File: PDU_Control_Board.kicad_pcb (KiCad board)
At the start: 4 copper layers, 237.7 x 87.4 mm, 221 parts, among them J1 Current_Sensor, J10 Precharge_2, J11 Shunt_2, J12 VIN_Enable, J13 To_Main_Connector, J2 Shunt_1, J20 VDC_IN, J21 VDC_OUT1, J22 VDC_OUT2, J3 SWD, J4 Precharge_1, J5 Precharge_2, J6 Shunt_2, J7 VIN_Enable, J8 Precharge_1, J9 Shunt_1, Q1 BSP75N, Q10 BC817, Q2 BSP75N, Q3 BSP75N, Q4 BSP75N, Q5 BSP75N, Q6 BC817, Q7 BC817, Q8 BC817, Q9 BC817, U1 LMV321, U2 APM32F405xG, U3 LMV321, U4 LMV321, U5 LMV321, U6 LMV321, Y2 X322516MOB4SI

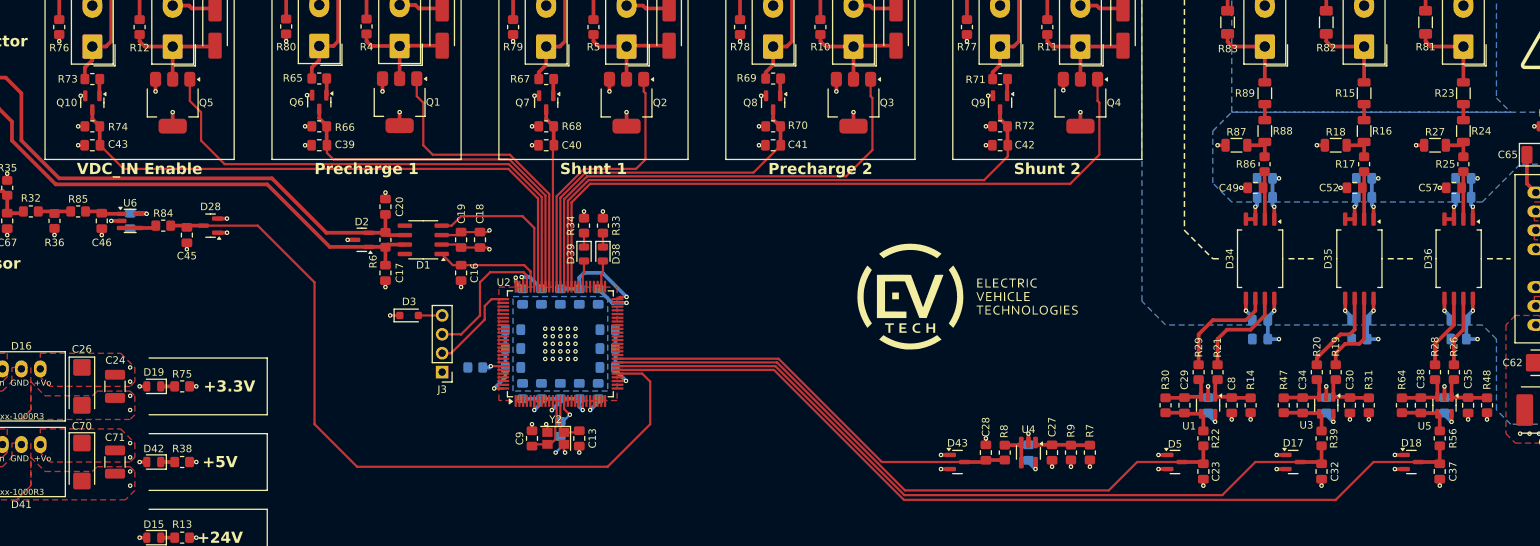
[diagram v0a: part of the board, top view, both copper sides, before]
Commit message: VER3.0: разобрался с бомом, добавил дискреты, DAC, поменял обратную свзять от контакторов, удлинил цепочку измерения высокого
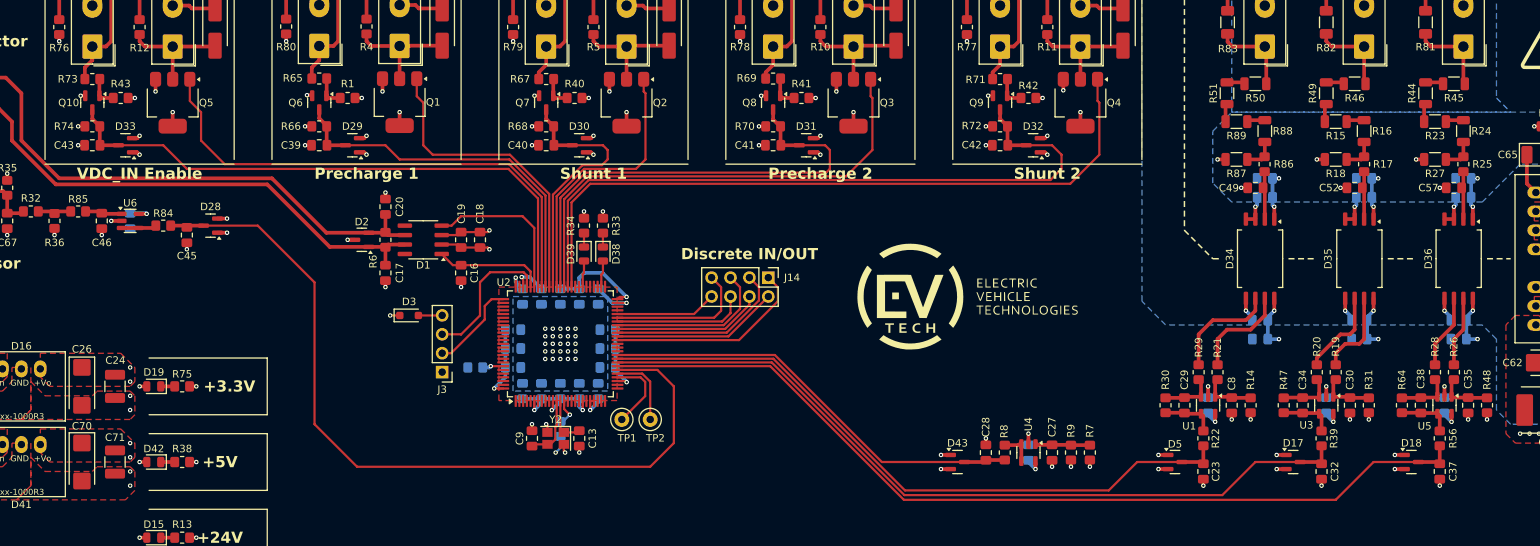
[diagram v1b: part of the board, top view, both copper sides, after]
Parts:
- added D29: ~, Package_TO_SOT_SMD:SOT-23, F.Cu at (282.6, 188.6)
- added D30: ~, Package_TO_SOT_SMD:SOT-23, F.Cu at (313.1, 188.6)
- added D31: ~, Package_TO_SOT_SMD:SOT-23, F.Cu at (343.5, 188.6)
- added D32: ~, Package_TO_SOT_SMD:SOT-23, F.Cu at (374.0, 188.6)
- added D33: ~, Package_TO_SOT_SMD:SOT-23, F.Cu at (252.1, 188.6)
- added J14: ~, Connector_PinHeader_2.54mm:PinHeader_2x04_P2.54mm_Vertical, F.Cu at (338.4, 206.4)
- added R1: 10k, Resistor_SMD:R_0805_2012Metric_Pad1.20x1.40mm_HandSolder, F.Cu at (281.9, 182.2)
- added R40: 10k, Resistor_SMD:R_0805_2012Metric_Pad1.20x1.40mm_HandSolder, F.Cu at (312.4, 182.2)
- added R41: 10k, Resistor_SMD:R_0805_2012Metric_Pad1.20x1.40mm_HandSolder, F.Cu at (342.9, 182.2)
- added R42: 10k, Resistor_SMD:R_0805_2012Metric_Pad1.20x1.40mm_HandSolder, F.Cu at (373.4, 182.2)
- added R43: 10k, Resistor_SMD:R_0805_2012Metric_Pad1.20x1.40mm_HandSolder, F.Cu at (251.5, 182.2)
- added R44: 23.7k, Resistor_SMD:R_1206_3216Metric, F.Cu at (426.7, 181.6)
- added R45: 23.7k, Resistor_SMD:R_1206_3216Metric, F.Cu at (430.5, 180.3)
- added R46: 23.7k, Resistor_SMD:R_1206_3216Metric, F.Cu at (417.2, 180.3)
- added R49: 23.7k, Resistor_SMD:R_1206_3216Metric, F.Cu at (413.4, 181.6)
- added R50: 23.7k, Resistor_SMD:R_1206_3216Metric, F.Cu at (403.9, 180.3)
- added R51: 23.7k, Resistor_SMD:R_1206_3216Metric, F.Cu at (400.1, 181.6)
- added TP1: TestPoint, TestPoint:TestPoint_Loop_D1.80mm_Drill1.0mm_Beaded, F.Cu at (318.8, 225.4)
- added TP2: TestPoint, TestPoint:TestPoint_Loop_D1.80mm_Drill1.0mm_Beaded, F.Cu at (322.6, 225.4)
- C39, C40, C41, C42, C43: value 2.2u -> 1u
- D1: value SIT65HVD232DR -> ~
- D10, D11, D12, D14, D15, D19, D20, D21, D22, D23, D24, D25, D26, D27, D38, D39, D40, D42, D9: value LED_Small -> ~
- D13, D3, D4, D6, D7, D8: value D_Small -> ~
- D16: value K7803-1000R3 -> ~
- D17, D18, D28, D43, D5: value BAT54S -> ~
- D2: value PESD2CAN -> ~
- D34, D35, D36: value NSI1311 -> ~
- D37: value WRB2403S-3WR2 -> ~
- D41: value K7805-1000R3 -> ~
- J1: value Current_Sensor -> ~
- J10, J5: value Precharge_2 -> ~
- J11, J6: value Shunt_2 -> ~
- J12, J7: value VIN_Enable -> ~
- J13: value To_Main_Connector -> ~
- J2, J9: value Shunt_1 -> ~
- J20: value VDC_IN -> ~
- J21: value VDC_OUT1 -> ~
- J22: value VDC_OUT2 -> ~
- J3: value SWD -> ~
- J4, J8: value Precharge_1 -> ~
- Q1, Q2, Q3, Q4, Q5: value BSP75N -> ~
- Q10, Q6, Q7, Q8, Q9: value BC817 -> ~
- R15, R16, R23, R24, R88, R89: value 47k -> 23.7k
- R18, R27, R87: value 240 -> 210
- R35: value DNP -> 1k
- R65, R67, R69, R71, R73: value 2.2k -> 10k
- R66, R68, R70, R72, R74: value 1k -> 100
- U1, U3, U5, U6: value LMV321 -> ~
- U2: value APM32F405xG -> ~
- U4: value LMV321 -> ~; footprint Package_TO_SOT_SMD:SOT-23-5_HandSoldering -> Package_TO_SOT_SMD:SOT-23-5
- Y2: value X322516MOB4SI -> ~
- moved R15 5.39 mm to (414.7, 185.4), turned to 180 degrees
- moved R23 5.39 mm to (428.0, 185.4), turned to 180 degrees
- moved R89 5.39 mm to (401.3, 185.4), turned to 180 degrees
- moved R18 1.91 mm to (414.7, 190.5)
- moved R27 1.91 mm to (428.0, 190.5)
- moved R87 1.91 mm to (401.3, 190.5)
- moved Q6 0.07 mm to (278.1, 182.9)
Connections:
- C28 pad 1: DC_Voltage_MCU -> +24V_SENSE
- D43 pad 3: DC_Voltage_MCU -> +24V_SENSE
- R15 pad 2: VDC_OUT1 -> Net-(R15-Pad2)
- R23 pad 2: VDC_OUT2 -> Net-(R23-Pad2)
- R8 pad 2: DC_Voltage_MCU -> +24V_SENSE
- R89 pad 2: VDC_IN -> Net-(R51-Pad1)
- U2 pad 30: Current_SENSE -> DAC_OUT2
- U2 pad 31: VDC_OUT2_SENSE -> Current_SENSE
- U2 pad 32: VDC_OUT1_SENSE -> VDC_OUT2_SENSE
- U2 pad 33: VDC_IN_SENSE -> VDC_OUT1_SENSE
- U2 pad 34: DC_Voltage_MCU -> VDC_IN_SENSE
- U2 pad 35: unconnected-(U2-PB0-Pad35) -> +24V_SENSE
- U2 pad 39: unconnected-(U2-PE8-Pad39) -> Discete_1
- U2 pad 40: unconnected-(U2-PE9-Pad40) -> Discete_2
- U2 pad 41: unconnected-(U2-PE10-Pad41) -> Discete_3
- U2 pad 42: unconnected-(U2-PE11-Pad42) -> Discete_4
- U2 pad 43: unconnected-(U2-PE12-Pad43) -> Discete_5
- U2 pad 44: unconnected-(U2-PE13-Pad44) -> Discete_6
- U2 pad 45: unconnected-(U2-PE14-Pad45) -> Discete_7
- U2 pad 46: unconnected-(U2-PE15-Pad46) -> Discete_8
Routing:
- net +24V_SENSE: track 0.00 -> 58.1 mm
- net DC_Voltage_MCU: track 57.9 -> 0.00 mm
- net Discete_1: track 0.00 -> 27.4 mm
- net Discete_3: track 0.00 -> 24.4 mm
- net Discete_2: track 0.00 -> 22.5 mm
- net Discete_5: track 0.00 -> 22.1 mm
- net Discete_4: track 0.00 -> 20.2 mm
- net Discete_7: track 0.00 -> 19.3 mm
- net Discete_6: track 0.00 -> 17.9 mm
- net ~{Shunt_2_ON}: track 79.8 -> 94.5 mm
- net ~{Precharge_2_ON}: track 49.7 -> 64.3 mm
- net Discete_8: track 0.00 -> 13.6 mm
- net ~{Shunt_1_ON}: track 24.3 -> 35.8 mm
- net DAC_OUT1: track 0.00 -> 10.3 mm
- net GND: track 89.5 -> 99.6 mm, vias 106 -> 116
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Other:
- board text added: "Discrete IN/OUT"

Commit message: VER3.0: заказал плату в резоните
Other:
- board text added: "CANH"
- board text added: "CANL"
- board text added: "DAC1"
- board text added: "DAC2"
- board text added: "GND"
- board text added: "OUT"
- board text added: "SWCLK"
- board text added: "SWDIO"

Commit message: VER1.1: обновил полигоны, закинул в резонит черновик
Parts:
- H4: value MountingHole_Pad -> MountingHole
- turned H4 to 0 degrees
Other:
- board text added: "PDU Control Board VER1.1"
- board text removed: "PDU Control Board VER1.0"

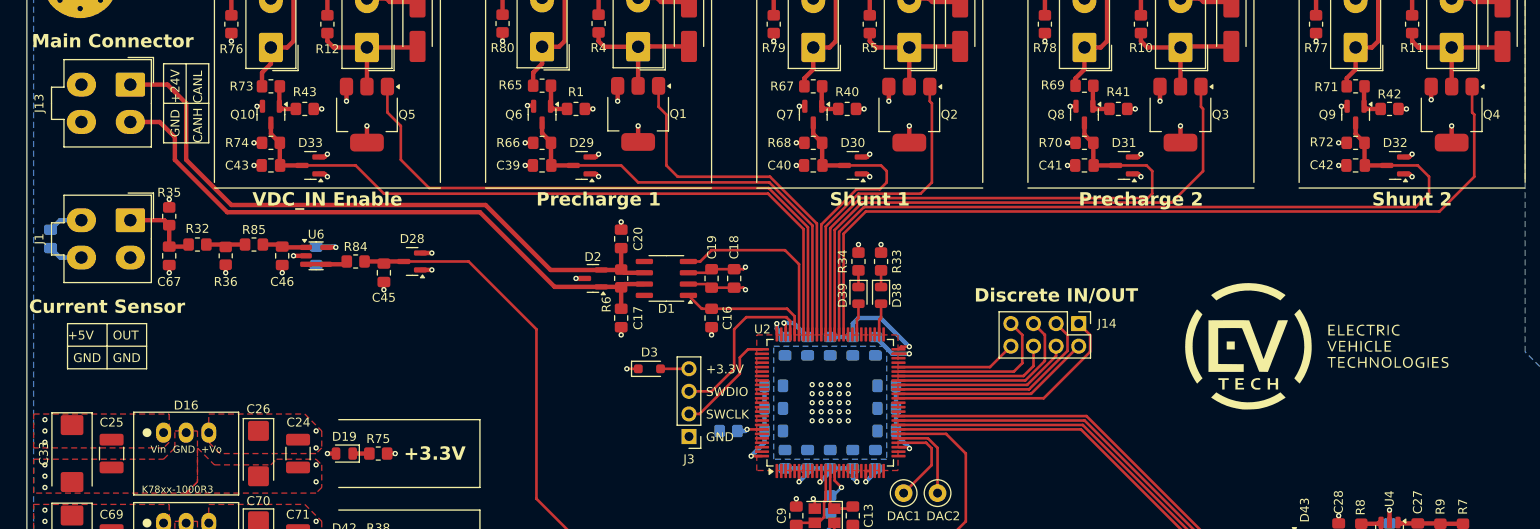
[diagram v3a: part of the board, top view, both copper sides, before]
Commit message: VER1.1: добавил схему предзаряда и защиту от переполюсовки по 24В
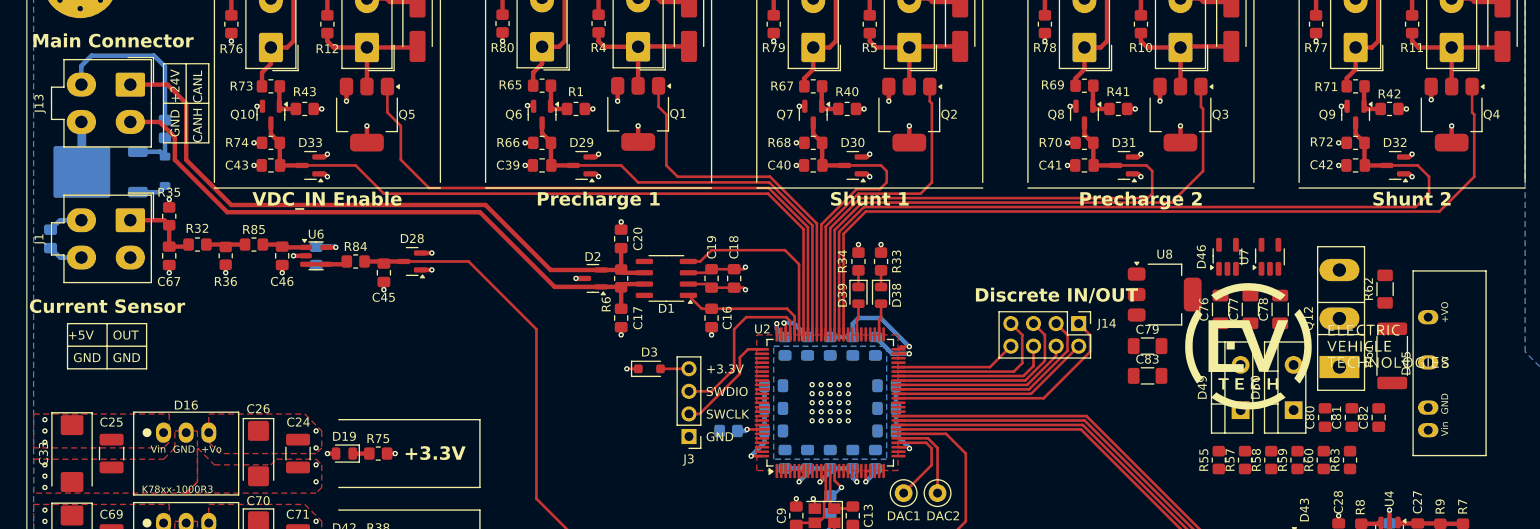
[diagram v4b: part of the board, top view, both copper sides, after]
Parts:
- added C76: 4.7u, Capacitor_SMD:C_1206_3216Metric_Pad1.33x1.80mm_HandSolder, F.Cu at (354.4, 204.8)
- added C77: 4.7u, Capacitor_SMD:C_1206_3216Metric_Pad1.33x1.80mm_HandSolder, F.Cu at (357.7, 204.8)
- added C78: 10u, Capacitor_SMD:C_1206_3216Metric_Pad1.33x1.80mm_HandSolder, F.Cu at (361.1, 204.8)
- added C79: 10u, Capacitor_SMD:C_1206_3216Metric_Pad1.33x1.80mm_HandSolder, F.Cu at (346.2, 208.9)
- added C80: 100n, Capacitor_SMD:C_0805_2012Metric_Pad1.18x1.45mm_HandSolder, F.Cu at (366.1, 216.9)
- added C81: 5.6n, Capacitor_SMD:C_0805_2012Metric_Pad1.18x1.45mm_HandSolder, F.Cu at (369.1, 216.9)
- added C82: 5.6n, Capacitor_SMD:C_0805_2012Metric_Pad1.18x1.45mm_HandSolder, F.Cu at (372.2, 216.9)
- added C83: 10u, Capacitor_SMD:C_1206_3216Metric_Pad1.33x1.80mm_HandSolder, F.Cu at (346.2, 212.2)
- added D44: BZT52C10, Diode_SMD:D_SOD-123, B.Cu at (235.8, 189.2)
- added D45: ~, MORNSUN:B_S-2WR3, F.Cu at (377.7, 212.0)
- added D46: ~, Package_TO_SOT_SMD:SOT-23-5_HandSoldering, F.Cu at (355.2, 198.9)
- added D49: ~, Package_TO_SOT_THT:TO-220-2_Vertical, F.Cu at (356.6, 216.1)
- added D50: ~, Package_TO_SOT_THT:TO-220-2_Vertical, F.Cu at (362.6, 216.1)
- added Q11: ~, Package_TO_SOT_SMD:TO-252-2, B.Cu at (227.7, 189.3)
- added Q12: ~, Package_TO_SOT_THT:TO-247-3_Vertical, F.Cu at (367.8, 211.2)
- added R54: 100k, Resistor_SMD:R_0805_2012Metric_Pad1.20x1.40mm_HandSolder, B.Cu at (235.8, 184.5)
- added R55: 200, Resistor_SMD:R_0805_2012Metric_Pad1.20x1.40mm_HandSolder, F.Cu at (354.2, 221.7)
- added R57: 13.3k, Resistor_SMD:R_0805_2012Metric_Pad1.20x1.40mm_HandSolder, F.Cu at (357.1, 221.7)
- added R58: 200k, Resistor_SMD:R_0805_2012Metric_Pad1.20x1.40mm_HandSolder, F.Cu at (360.1, 221.7)
- added R59: 2.37k, Resistor_SMD:R_0805_2012Metric_Pad1.20x1.40mm_HandSolder, F.Cu at (363.0, 221.7)
- added R60: 10k, Resistor_SMD:R_0805_2012Metric_Pad1.20x1.40mm_HandSolder, F.Cu at (366.0, 221.7)
- added R61: 0.1, Resistor_SMD:R_2512_6332Metric_Pad1.40x3.35mm_HandSolder, F.Cu at (373.7, 210.0)
- added R62: 0, Resistor_SMD:R_1206_3216Metric_Pad1.30x1.75mm_HandSolder, F.Cu at (372.9, 202.5)
- added R63: 10k, Resistor_SMD:R_0805_2012Metric_Pad1.20x1.40mm_HandSolder, F.Cu at (368.9, 221.7)
- added U7: ~, Package_TO_SOT_SMD:SOT-23-5_HandSoldering, F.Cu at (359.9, 198.9)
- added U8: ~, Package_TO_SOT_SMD:SOT-223-3_TabPin2, F.Cu at (348.1, 203.1)
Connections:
- J13 pad 4: GND -> -24V
- R50 pad 2: VDC_IN -> VDC
- R83 pad 1: VDC_IN -> VDC
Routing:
- net +24V: track 60.0 -> 78.5 mm
- net -24V: track 0.00 -> 5.63 mm
- net Net-(D44-K): track 0.00 -> 5.38 mm
- net GND: track 99.6 -> 102.9 mm

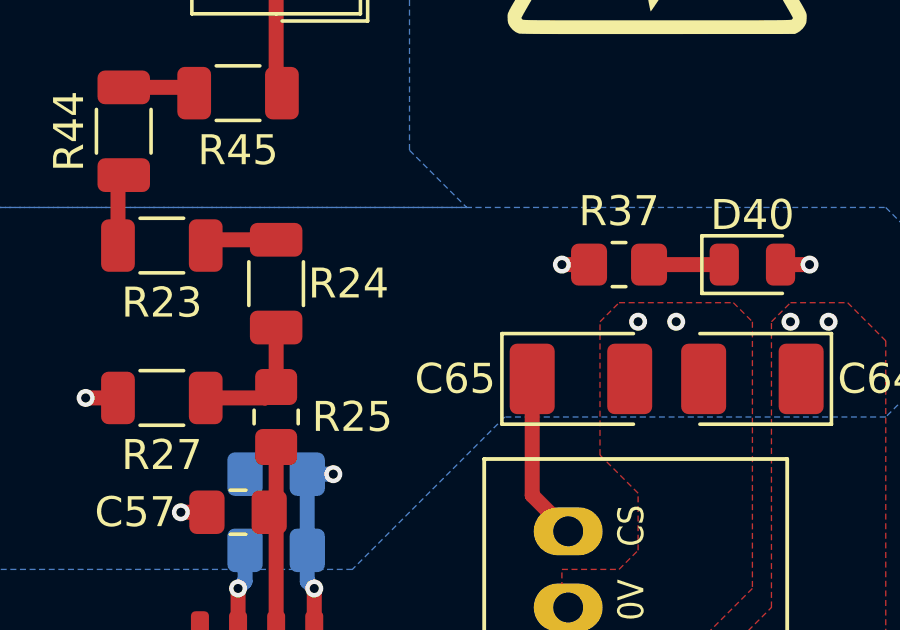
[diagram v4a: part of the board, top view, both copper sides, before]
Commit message: VER1.1: добавил резистор смещение в измерение шины DC
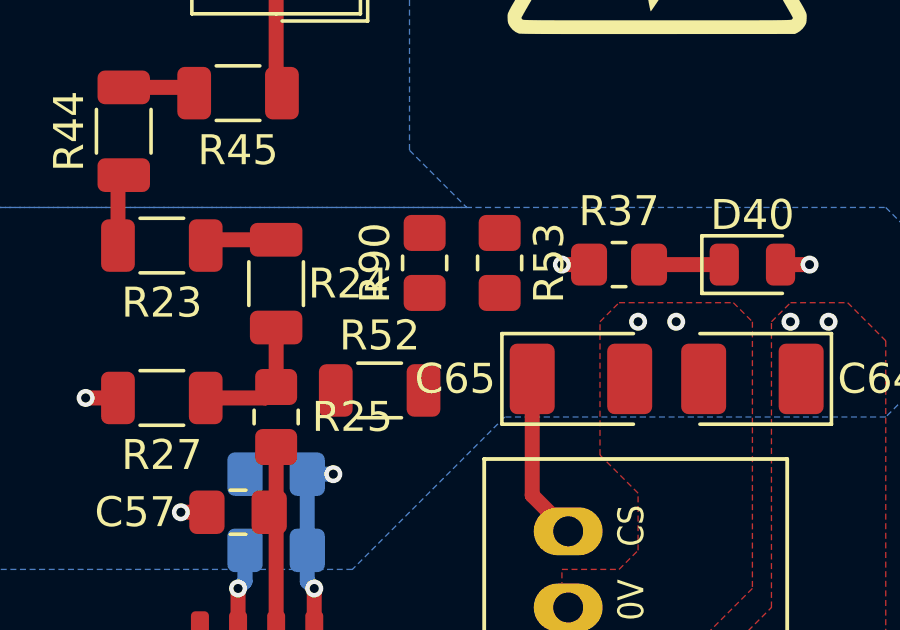
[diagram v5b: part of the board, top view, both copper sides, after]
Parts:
- added R52: 1k, Resistor_SMD:R_1206_3216Metric, F.Cu at (435.2, 190.2)
- added R53: 1k, Resistor_SMD:R_0805_2012Metric_Pad1.20x1.40mm_HandSolder, F.Cu at (439.2, 186.0)
- added R90: 2.32k, Resistor_SMD:R_0805_2012Metric_Pad1.20x1.40mm_HandSolder, F.Cu at (436.8, 186.0)
- R23, R24, R44, R45: value 23.7k -> 200k
- R27: value 210 -> 1k
